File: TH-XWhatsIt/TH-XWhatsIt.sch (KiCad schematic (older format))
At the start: 30 parts, among them J1 COLUMNS, J12 EXPANSION HEADER, J2 ROWS, U1 LM339, U2 MCP4921-EP, U3 74HCT595, U5 74HCT595, U6 LM339, U7 ProMicro, U8 74HCT595

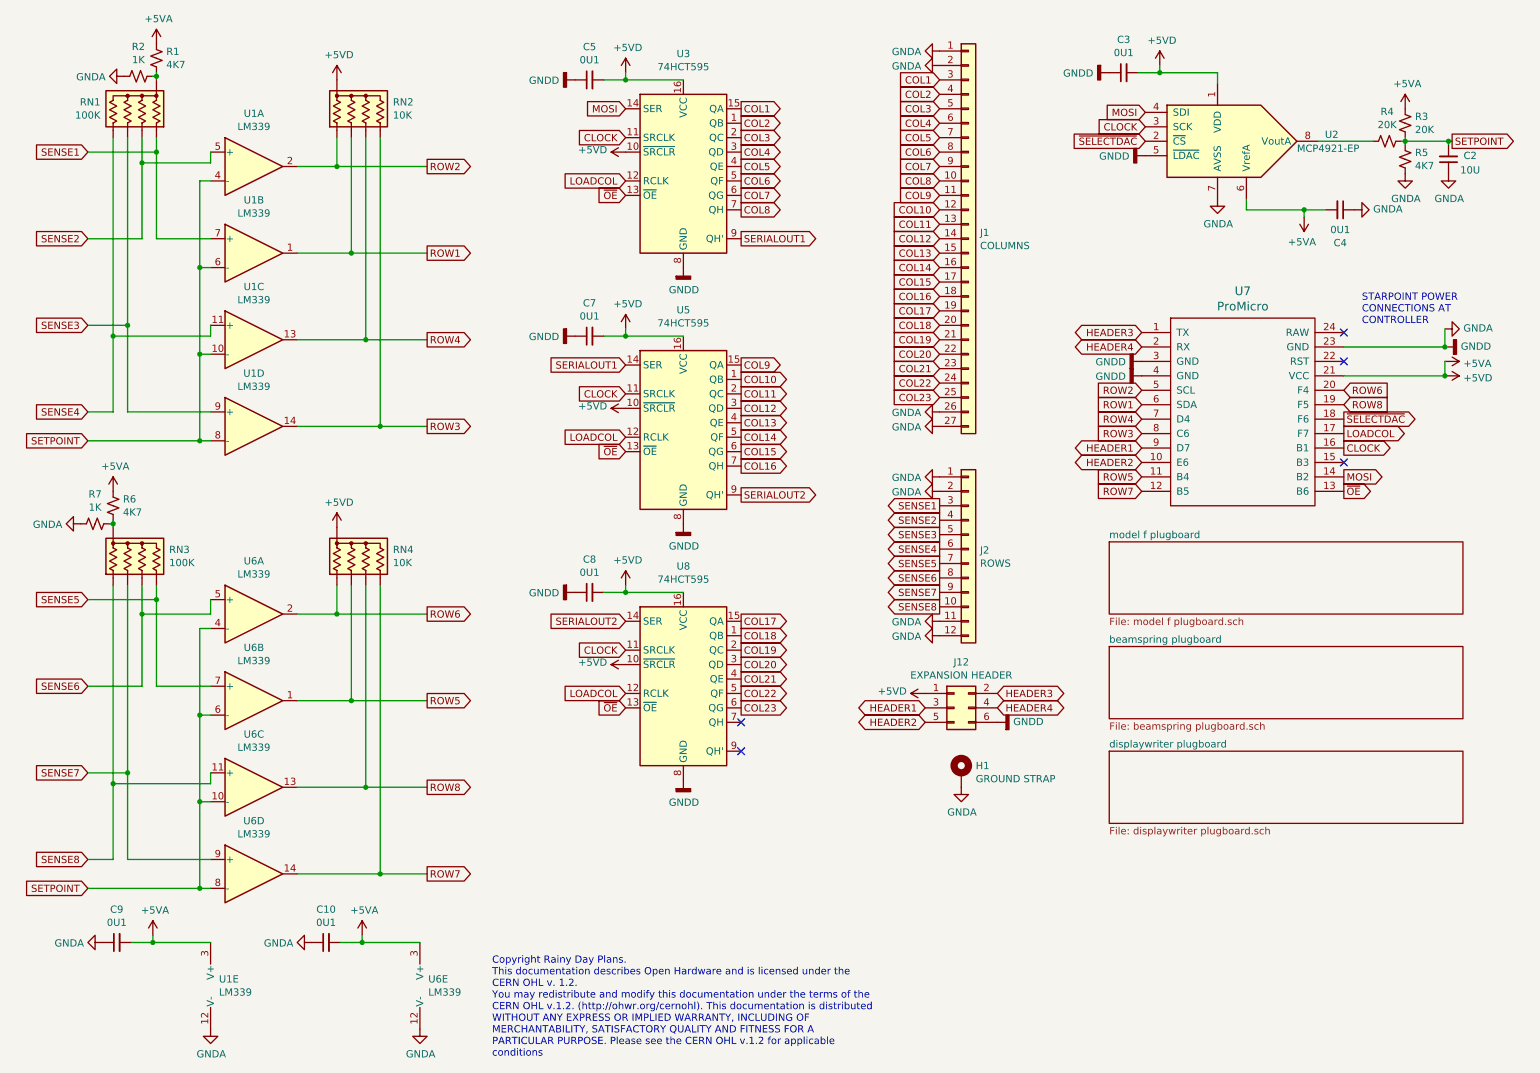
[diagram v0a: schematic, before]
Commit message: version bump to 2.0 due to header position changes finished wiring up most of the plugboards, but displaywriter as per usual is the most annoying.....see changes file for more details (jan 3rd, 2020)
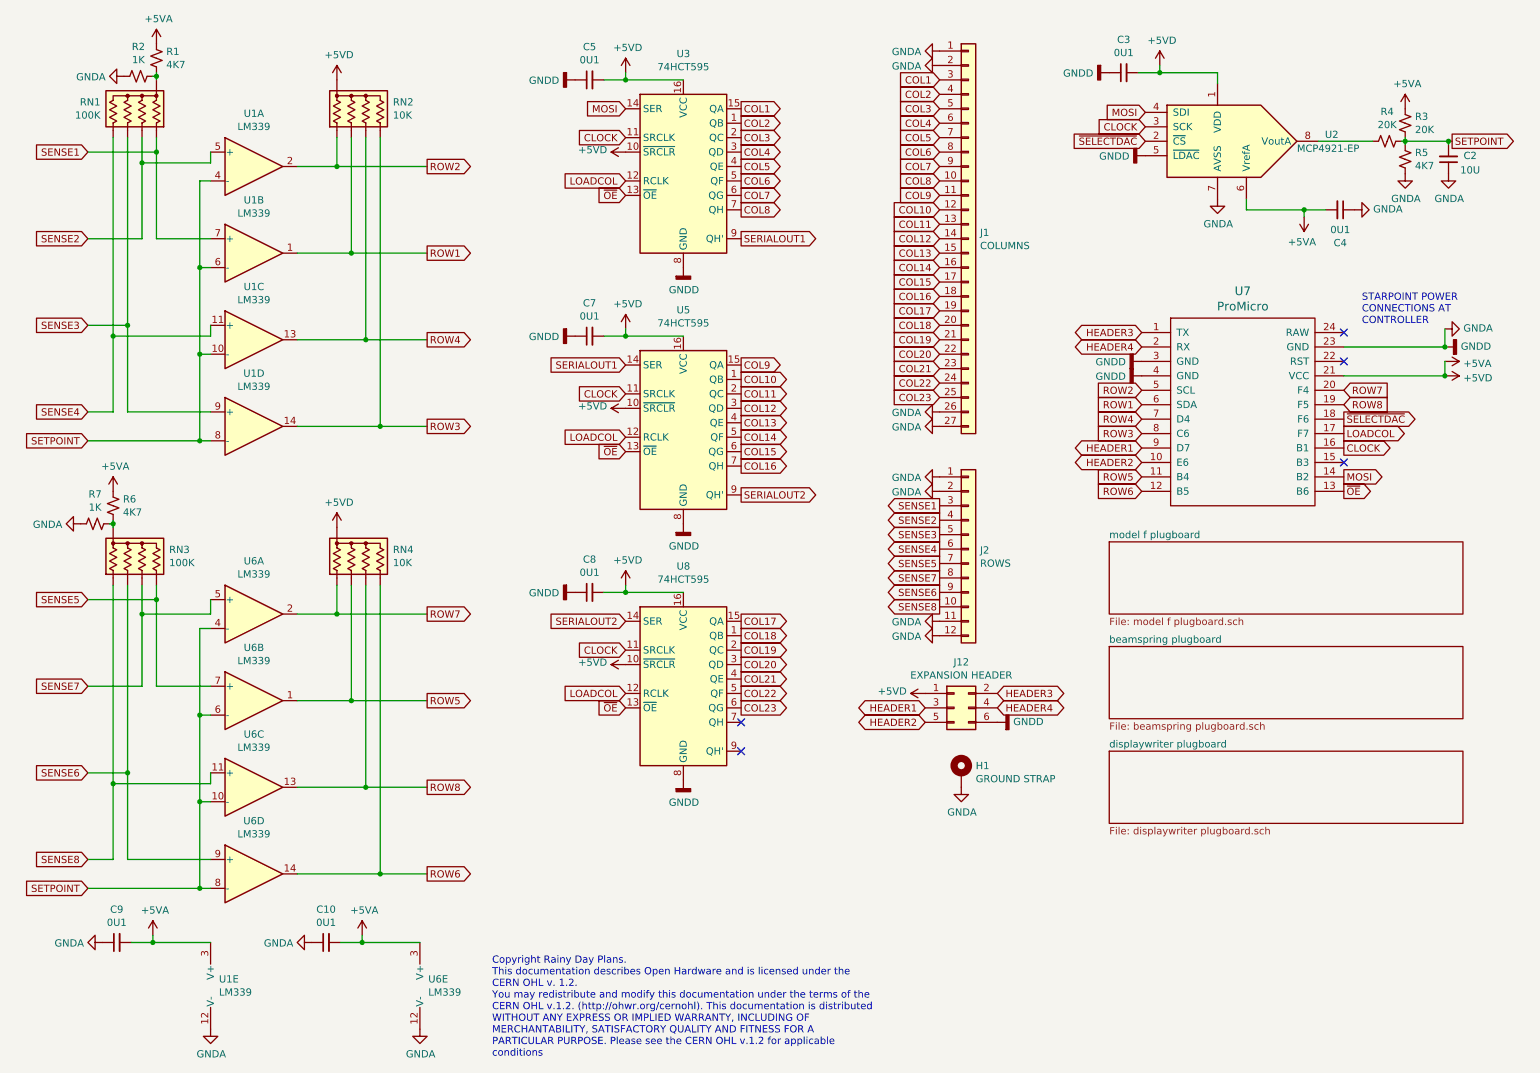
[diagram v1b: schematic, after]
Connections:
- net ROW6: now also RN4.5 (R4), U6.14, U7.12 (B5); no longer RN4.2 (R1), U6.2, U7.20 (F4)
- net ROW7: now also RN4.2 (R1), U6.2, U7.20 (F4); no longer RN4.5 (R4), U6.14, U7.12 (B5)
- net SENSE6: now also J2.9 (Pin_9), RN3.3 (R2), U6.9 (+); no longer J2.8 (Pin_8), RN3.4 (R3), U6.5 (+)
- net SENSE7: now also J2.8 (Pin_8), RN3.4 (R3), U6.5 (+); no longer J2.9 (Pin_9), RN3.3 (R2), U6.9 (+)
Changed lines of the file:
@@
 EESchema Schematic File Version 4
+LIBS:TH-XWhatsIt-cache
 EELAYER 30 0
 EELAYER END
@@
 Title "THT-XWhatsIt combined beamspring and model f controller"
 Date "2020-01-31"
-Rev "0.0.1"
+Rev "0.0.2"
 Comp "Rainy Day Plans"
 Comment1 ""
@@
 Text GLabel 8450 3725 0    50   Input ~ 0
 ROW5
+Text GLabel 8450 3825 0    50   Input ~ 0
+ROW6
 Text GLabel 9850 3125 2    50   Input ~ 0
-ROW6
-Text GLabel 8450 3825 0    50   Input ~ 0
 ROW7
 Text GLabel 9850 3225 2    50   Input ~ 0
@@
 Text GLabel 3500 5275 2    50   Output ~ 0
 ROW5
-Text GLabel 3500 4675 2    50   Output ~ 0
+Text GLabel 3500 6475 2    50   Output ~ 0
 ROW6
 Text GLabel 1150 4575 0    50   Input ~ 0
 SENSE5
-Text GLabel 1150 5175 0    50   Input ~ 0
+Text GLabel 1150 5775 0    50   Input ~ 0
 SENSE6
 $Comp
@@
 Wire Wire Line
 	1525 5175 1525 4675
-Text GLabel 1150 5775 0    50   Input ~ 0
+Text GLabel 1150 5175 0    50   Input ~ 0
 SENSE7
 Wire Wire Line
@@
 Text GLabel 3500 5875 2    50   Output ~ 0
 ROW8
-Text GLabel 3500 6475 2    50   Output ~ 0
+Text GLabel 3500 4675 2    50   Output ~ 0
 ROW7
 Wire Wire Line
@@
 Text GLabel 7050 4325 0    50   Output ~ 0
 SENSE5
+Text GLabel 7050 4525 0    50   Output ~ 0
+SENSE6
 Text GLabel 7050 4425 0    50   Output ~ 0
-SENSE6
-Text GLabel 7050 4525 0    50   Output ~ 0
 SENSE7
 Text GLabel 7050 4625 0    50   Output ~ 0

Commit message: rumors of my demise are greatly exaggerated, updates; more incoming now powered with new pc! thanks for being patient, please inform of futher changes!
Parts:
- removed C2: 10U, Capacitor_THT:C_Disc_D3.0mm_W1.6mm_P2.50mm, symbol Device:C_Small
- U7: symbol promicro:ProMicro -> TH-XWhatsIt-rescue:ProMicro-promicro
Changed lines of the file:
@@
 EESchema Schematic File Version 4
-LIBS:TH-XWhatsIt-cache
 EELAYER 30 0
 EELAYER END
@@
 Wire Wire Line
 	10275 1400 10275 1425
-Text GLabel 10600 1400 2    50   Output ~ 0
-SETPOINT
 Wire Wire Line
 	1925 6575 1150 6575
@@
 CLOCK
 $Comp
-L promicro:ProMicro U7
+L TH-XWhatsIt-rescue:ProMicro-promicro U7
 U 1 1 5E3248FF
 P 9150 3475
@@
 	0    1    1    0
 $EndComp
-$Comp
-L Device:C_Small C2
-U 1 1 5E35E372
-P 10575 1525
-F 0 "C2" H 10725 1500 50  0000 C CNN
-F 1 "10U" H 10725 1600 50  0000 C CNN
-F 2 "Capacitor_THT:C_Disc_D3.0mm_W1.6mm_P2.50mm" H 10575 1525 50  0001 C CNN
-F 3 "~" H 10575 1525 50  0001 C CNN
-	1    10575 1525
-	1    0    0    1
-$EndComp
 Wire Wire Line
 	8975 925  8975 1000
@@
 	0    -1   -1   0
 $EndComp
-Wire Wire Line
-	10575 1425 10575 1400
-Wire Wire Line
-	10575 1400 10600 1400
-Connection ~ 10575 1400
-Wire Wire Line
-	10275 1400 10575 1400
 Text GLabel 1150 6375 0    50   Input ~ 0
 SENSE8
@@
 F 3 "" H 5275 5825 50  0001 C CNN
 	1    5275 5825
-	1    0    0    -1
-$EndComp
-$Comp
-L power:GNDA #PWR0127
-U 1 1 5E834F91
-P 10575 1625
-F 0 "#PWR0127" H 10575 1375 50  0001 C CNN
-F 1 "GNDA" H 10580 1452 50  0000 C CNN
-F 2 "" H 10575 1625 50  0001 C CNN
-F 3 "" H 10575 1625 50  0001 C CNN
-	1    10575 1625
 	1    0    0    -1
 $EndComp
@@
 Text Notes 3950 7750 0    50   ~ 0
 Copyright Rainy Day Plans.\nThis documentation describes Open Hardware and is licensed under the\nCERN OHL v. 1.2.\nYou may redistribute and modify this documentation under the terms of the\nCERN OHL v.1.2. (http://ohwr.org/cernohl). This documentation is distributed\nWITHOUT ANY EXPRESS OR IMPLIED WARRANTY, INCLUDING OF\nMERCHANTABILITY, SATISFACTORY QUALITY AND FITNESS FOR A\nPARTICULAR PURPOSE. Please see the CERN OHL v.1.2 for applicable\nconditions
+Text GLabel 10600 1400 2    50   Output ~ 0
+SETPOINT
+Wire Wire Line
+	10275 1400 10600 1400
 $EndSCHEMATC

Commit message: Get rid of the rescue library
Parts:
- U7: symbol TH-XWhatsIt-rescue:ProMicro-promicro -> promicro:ProMicro
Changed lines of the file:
@@
 CLOCK
 $Comp
-L TH-XWhatsIt-rescue:ProMicro-promicro U7
+L promicro:ProMicro U7
 U 1 1 5E3248FF
 P 9150 3475

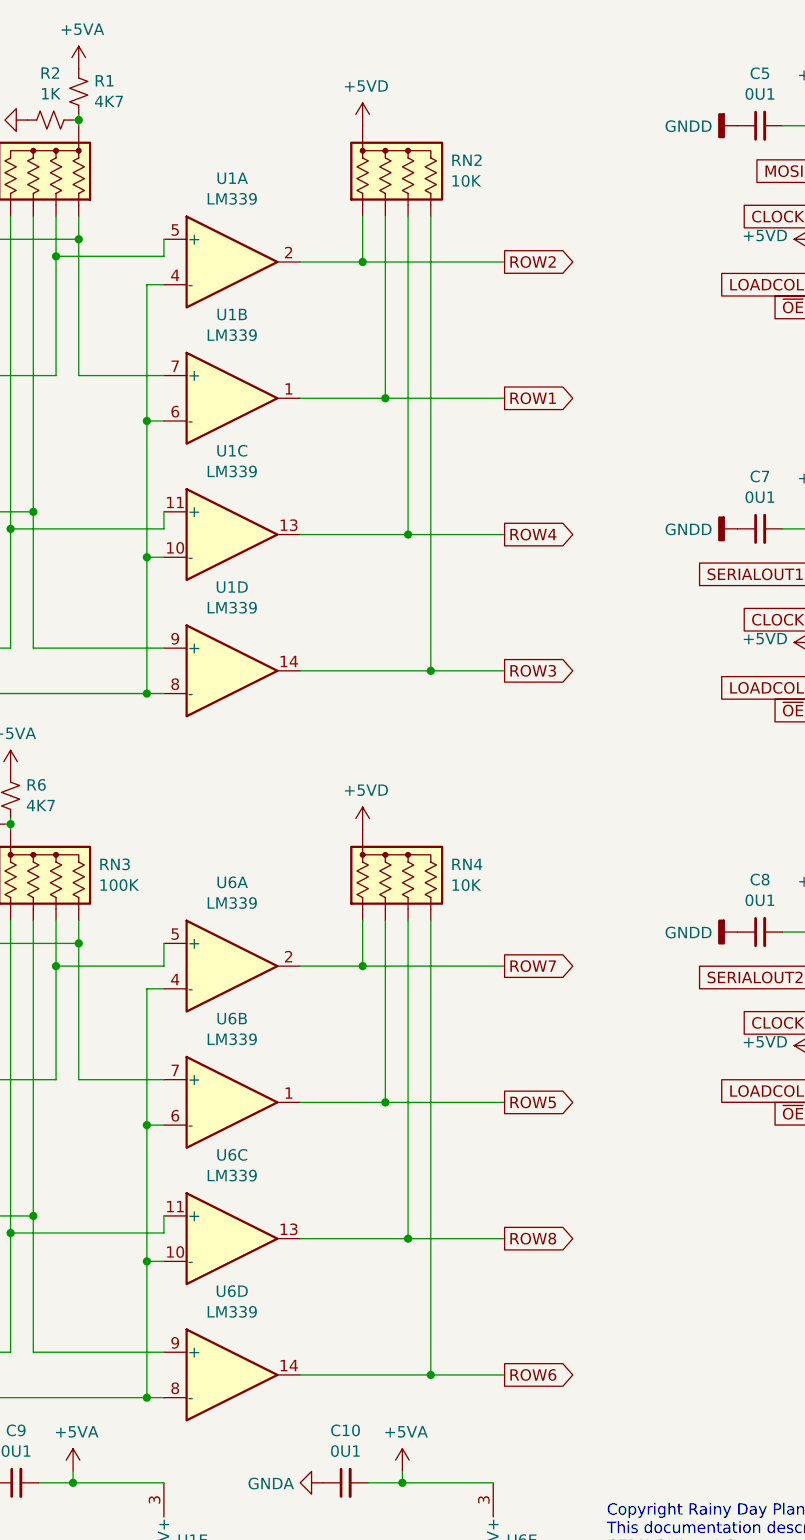
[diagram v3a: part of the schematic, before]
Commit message: Removed pull-ups from LM339 outputs. These will be provided in the atmega from now on.
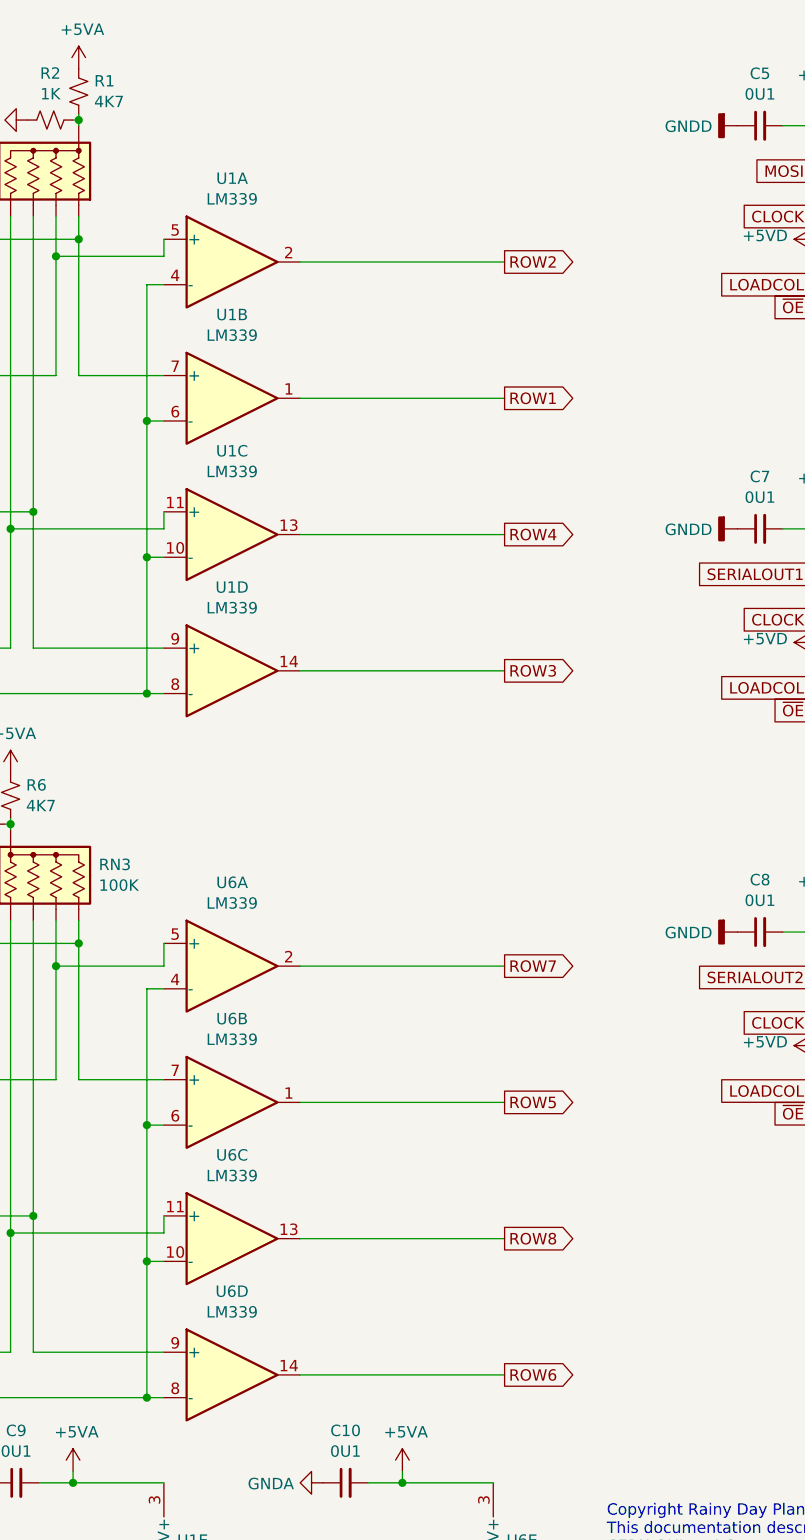
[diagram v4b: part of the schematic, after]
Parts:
- removed RN2, RN4: 10K, Resistor_THT:R_Array_SIP5, symbol Device:R_Network04_US
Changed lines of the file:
@@
 ~OE
-$Comp
-L Device:R_Network04_US RN4
-U 1 1 5E3332D9
-P 3075 4275
-F 0 "RN4" H 3263 4321 50  0000 L CNN
-F 1 "10K" H 3263 4230 50  0000 L CNN
-F 2 "Resistor_THT:R_Array_SIP5" V 3350 4275 50  0001 C CNN
-F 3 "http://www.vishay.com/docs/31509/csc.pdf" H 3075 4275 50  0001 C CNN
-	1    3075 4275
-	1    0    0    -1
-$EndComp
 $Comp
 L Device:R_Network04_US RN3
@@
 Wire Wire Line
 	1600 6900 1600 6950
-Wire Wire Line
-	2600 4675 2875 4675
-Wire Wire Line
-	2875 4675 2875 4475
-Wire Wire Line
-	2975 5275 2975 4475
-Wire Wire Line
-	2600 5275 2975 5275
-Wire Wire Line
-	3075 4475 3075 5875
-Wire Wire Line
-	2600 5875 3075 5875
-Wire Wire Line
-	3175 6475 3175 4475
-Wire Wire Line
-	2600 6475 3175 6475
 $Comp
 L Device:R_Small_US R4
@@
 NoConn ~ 9850 2725
 NoConn ~ 9850 2925
-Wire Wire Line
-	2875 4675 3500 4675
-Connection ~ 2875 4675
-Wire Wire Line
-	2975 5275 3500 5275
-Connection ~ 2975 5275
-Wire Wire Line
-	3075 5875 3500 5875
-Connection ~ 3075 5875
-Wire Wire Line
-	3175 6475 3500 6475
-Connection ~ 3175 6475
 Text GLabel 8450 3225 0    50   Input ~ 0
 ROW1
@@
 $EndComp
 $Comp
-L Device:R_Network04_US RN2
-U 1 1 5E3E3851
-P 3075 1175
-F 0 "RN2" H 3263 1221 50  0000 L CNN
-F 1 "10K" H 3263 1130 50  0000 L CNN
-F 2 "Resistor_THT:R_Array_SIP5" V 3350 1175 50  0001 C CNN
-F 3 "http://www.vishay.com/docs/31509/csc.pdf" H 3075 1175 50  0001 C CNN
-	1    3075 1175
-	1    0    0    -1
-$EndComp
-$Comp
 L Device:R_Network04_US RN1
 U 1 1 5E3E3857
@@
 SENSE4
 Wire Wire Line
-	2600 1575 2875 1575
-Wire Wire Line
-	2875 1575 2875 1375
-Wire Wire Line
-	2975 2175 2975 1375
-Wire Wire Line
-	2600 2175 2975 2175
-Wire Wire Line
-	3075 1375 3075 2775
-Wire Wire Line
-	2600 2775 3075 2775
-Wire Wire Line
-	3175 3375 3175 1375
-Wire Wire Line
-	2600 3375 3175 3375
-Wire Wire Line
 	1925 3475 1150 3475
 Connection ~ 1925 3475
 Text GLabel 1150 3475 0    50   Input ~ 0
 SETPOINT
-Wire Wire Line
-	2875 1575 3500 1575
-Connection ~ 2875 1575
-Wire Wire Line
-	2975 2175 3500 2175
-Connection ~ 2975 2175
-Wire Wire Line
-	3075 2775 3500 2775
-Connection ~ 3075 2775
-Wire Wire Line
-	3175 3375 3500 3375
-Connection ~ 3175 3375
 Text GLabel 3500 2175 2    50   Output ~ 0
 ROW1
@@
 $EndComp
 $Comp
-L power:+5VD #PWR0104
-U 1 1 5E81684F
-P 2875 4075
-F 0 "#PWR0104" H 2875 3925 50  0001 C CNN
-F 1 "+5VD" H 2890 4248 50  0000 C CNN
-F 2 "" H 2875 4075 50  0001 C CNN
-F 3 "" H 2875 4075 50  0001 C CNN
-	1    2875 4075
-	1    0    0    -1
-$EndComp
-$Comp
-L power:+5VD #PWR0105
-U 1 1 5E817368
-P 2875 975
-F 0 "#PWR0105" H 2875 825 50  0001 C CNN
-F 1 "+5VD" H 2890 1148 50  0000 C CNN
-F 2 "" H 2875 975 50  0001 C CNN
-F 3 "" H 2875 975 50  0001 C CNN
-	1    2875 975
-	1    0    0    -1
-$EndComp
-$Comp
 L power:+5VD #PWR0106
 U 1 1 5E817D6B
@@
 Wire Wire Line
 	10275 1400 10600 1400
+Wire Wire Line
+	2600 1575 3500 1575
+Wire Wire Line
+	2600 2175 3500 2175
+Wire Wire Line
+	2600 2775 3500 2775
+Wire Wire Line
+	2600 3375 3500 3375
+Wire Wire Line
+	2600 4675 3500 4675
+Wire Wire Line
+	2600 5275 3500 5275
+Wire Wire Line
+	2600 5875 3500 5875
+Wire Wire Line
+	2600 6475 3500 6475
 $EndSCHEMATC
